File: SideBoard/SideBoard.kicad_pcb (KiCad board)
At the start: 2 copper layers, 22 parts, among them J1 RJ45, J2 RJ12

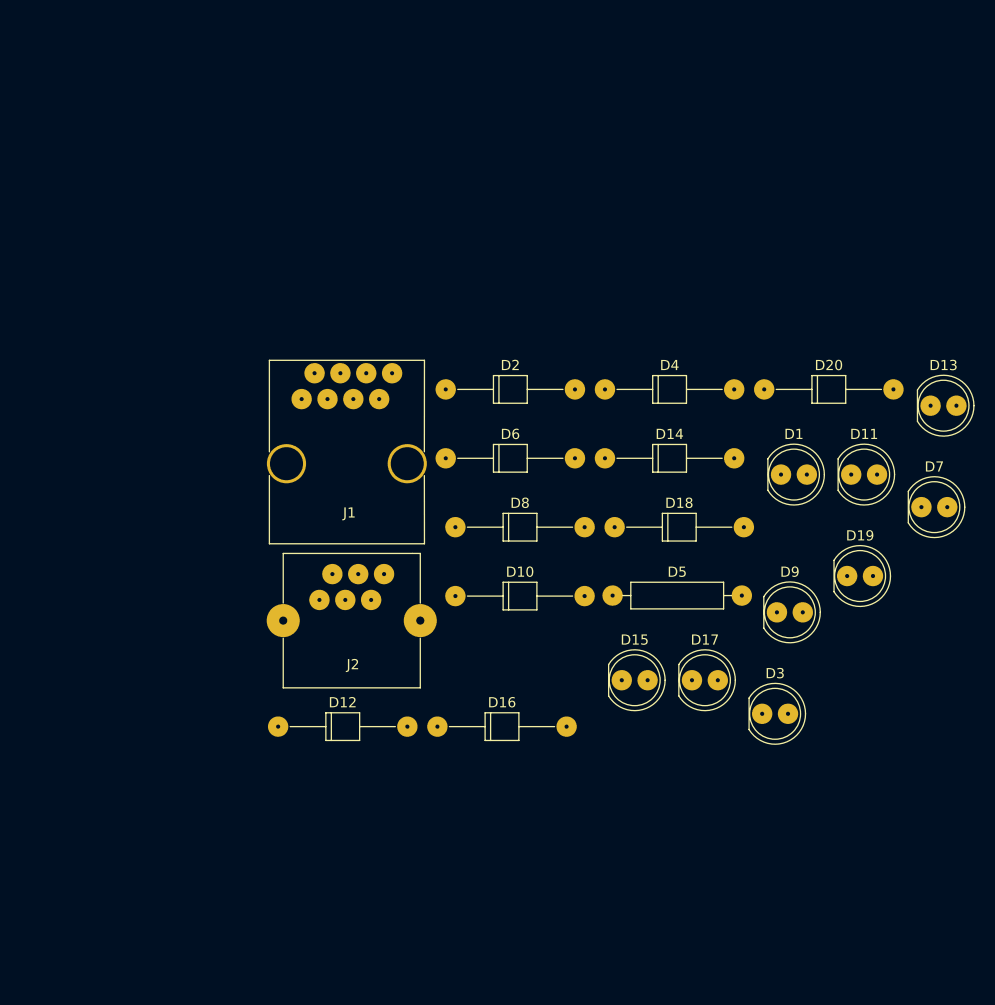
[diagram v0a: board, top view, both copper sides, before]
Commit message: Correct mistakes on SideBoard + begin routing
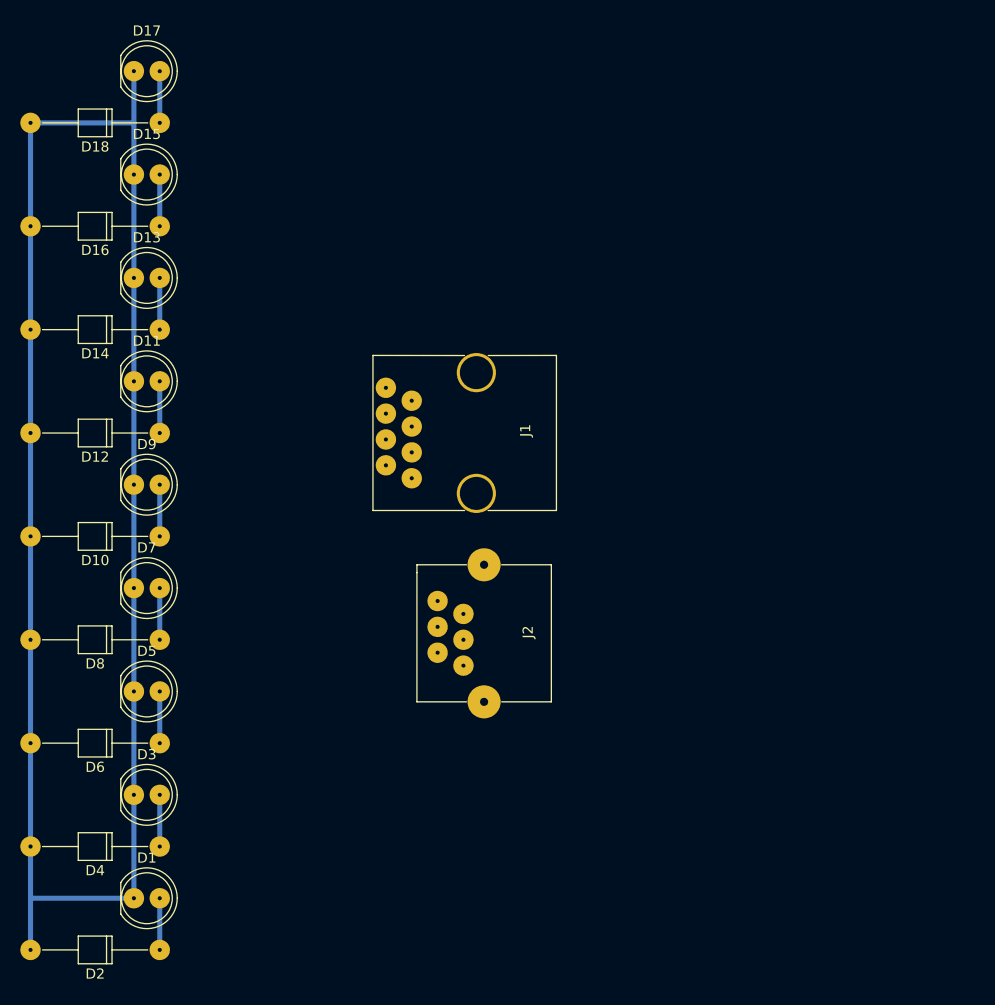
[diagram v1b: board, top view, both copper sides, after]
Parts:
- removed D19: LED, std_lib_SRC:LED_D5.0mm
- removed D20: 1N4148, std_lib_SRC:Diode
- D5: footprint std_lib_SRC:Resistor -> std_lib_SRC:LED_D5.0mm
- moved D17 81.2 mm to (135.9, 58.4)
- moved D13 79.3 mm to (135.9, 78.7)
- moved D7 77.8 mm to (135.9, 109.2)
- moved D1 76.0 mm to (135.9, 139.7)
- moved D11 71.1 mm to (135.9, 88.9)
- moved D15 69.1 mm to (135.9, 68.6)
- moved D9 64.4 mm to (135.9, 99.1)
- moved D4 62.7 mm to (138.4, 134.6), turned to 180 degrees
- moved D3 62.3 mm to (135.9, 129.5)
- moved D2 61.8 mm to (138.4, 144.8), turned to 180 degrees
- moved D18 59.8 mm to (138.4, 63.5), turned to 180 degrees
- moved D16 56.2 mm to (138.4, 73.7), turned to 180 degrees
- moved D5 48.0 mm to (135.9, 119.4)
- moved D14 45.5 mm to (138.4, 83.8), turned to 180 degrees
- moved D6 39.7 mm to (138.4, 124.5), turned to 180 degrees
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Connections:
- D10 pad 1: P4 -> P5
- D11 pad 2: P5 -> P6
- D12 pad 1: P5 -> P6
- D13 pad 2: P6 -> P7
- D14 pad 1: P6 -> P7
- D15 pad 2: P7 -> P8
- D16 pad 1: P7 -> P8
- D17 pad 2: P8 -> P9
- D18 pad 1: P8 -> P9
- D7 pad 2: P3 -> P4
- D8 pad 1: P3 -> P4
- D9 pad 2: P4 -> P5
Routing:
- net Net-(D1-Pad1): track 0.00 -> 182.9 mm
- net P2: track 0.00 -> 5.08 mm
- net P1: track 0.00 -> 5.08 mm
- net P9: track 0.00 -> 5.08 mm
- net P8: track 0.00 -> 5.08 mm
- net P7: track 0.00 -> 5.08 mm
- net P6: track 0.00 -> 5.08 mm
- net P5: track 0.00 -> 5.08 mm
- net P4: track 0.00 -> 5.08 mm
- net P3: track 0.00 -> 5.08 mm
